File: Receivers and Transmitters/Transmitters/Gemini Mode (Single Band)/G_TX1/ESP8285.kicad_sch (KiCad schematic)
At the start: 22 parts, among them U4 ESP8285H16, Y2 26MHz

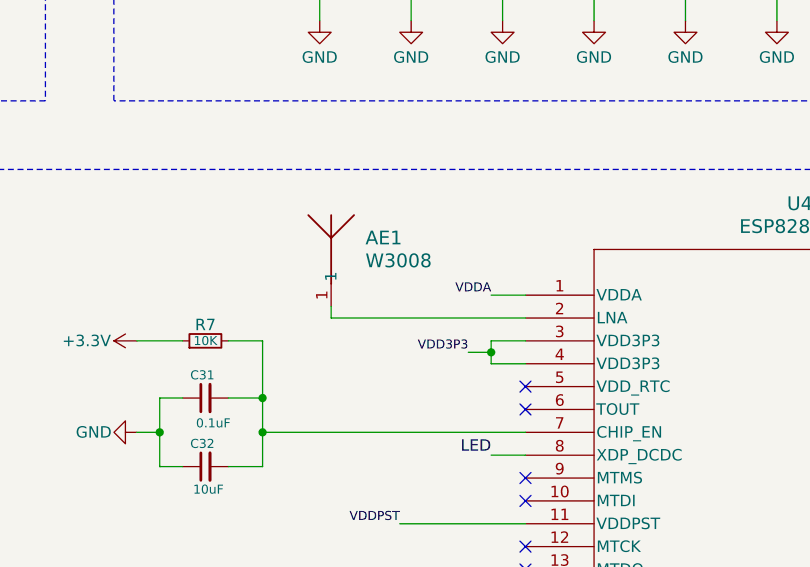
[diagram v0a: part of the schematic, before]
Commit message: Add Gemini Mode (Single Band) TX board image and documentation updates - Updated hardware setup to include Gemini TX - Added G_TX1_2.4G preview image - Updated KiCad schematic with LNA section and 5.6pF matching capacitor for 50Ω impedance - Modified PCB layout accordingly - Updated README and index.html with Gemini TX board references
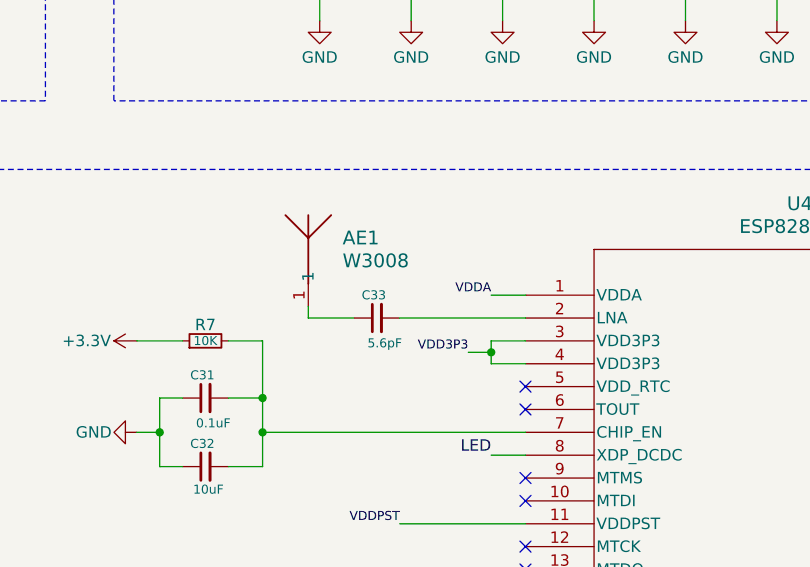
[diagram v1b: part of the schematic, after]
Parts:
- added C33: 5.6pF, Capacitor_SMD:C_01005_0402Metric_Pad0.57x0.30mm_HandSolder, symbol Device:C_Small
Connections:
- net at AE1.1: now also C33.1; no longer U4.2 (LNA)
- new net: C33.2, U4.2 (LNA)
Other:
- moved on the sheet: AE1
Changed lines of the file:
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@@
+	(wire
+		(pts
+			(xy 92.71 91.44) (xy 97.79 91.44)
+		)
+		(stroke
+			(width 0)
+			(type default)
+		)
+	)
 	(wire
 		(pts
@@
 	(wire
 		(pts
-			(xy 95.25 91.44) (xy 116.84 91.44)
-		)
-		(stroke
-			(width 0)
-			(type default)
-		)
-	)
-	(wire
-		(pts
 			(xy 78.74 107.95) (xy 76.2 107.95)
 		)
@@
 	(wire
 		(pts
+			(xy 102.87 91.44) (xy 116.84 91.44)
+		)
+		(stroke
+			(width 0)
+			(type default)
+		)
+	)
+	(wire
+		(pts
 			(xy 205.74 106.68) (xy 207.01 106.68)
 		)
@@
 	(wire
 		(pts
-			(xy 95.25 90.17) (xy 95.25 91.44)
+			(xy 92.71 90.17) (xy 92.71 91.44)
 		)
 		(stroke
@@
 	)
 	(symbol
+		(lib_id "Device:C_Small")
+		(at 100.33 91.44 90)
+		(unit 1)
+		(exclude_from_sim no)
+		(in_bom yes)
+		(on_board yes)
+		(dnp no)
+		(property "Reference" "C33"
+			(at 101.346 88.9 90)
+			(effects
+				(font
+					(size 1 1)
+				)
+				(justify left)
+			)
+		)
+		(property "Value" "5.6pF"
+			(at 103.124 94.234 90)
+			(effects
+				(font
+					(size 1 1)
+				)
+				(justify left)
+			)
+		)
+		(property "Footprint" "Capacitor_SMD:C_01005_0402Metric_Pad0.57x0.30mm_HandSolder"
+			(at 100.33 91.44 0)
+			(effects
+				(font
+					(size 1.27 1.27)
+				)
+				(hide yes)
+			)
+		)
+		(property "Datasheet" "~"
+			(at 100.33 91.44 0)
+			(effects
+				(font
+					(size 1.27 1.27)
+				)
+				(hide yes)
+			)
+		)
+		(property "Description" "Unpolarized capacitor, small symbol"
+			(at 100.33 91.44 0)
+			(effects
+				(font
+					(size 1.27 1.27)
+				)
+				(hide yes)
+			)
+		)
+		(pin "2"
+		)
+		(pin "1"
+		)
+		(instances
+			(project "G_TX1"
+				(path "/32640adb-d3ae-4079-8814-1903180e0e12/36e48682-81ba-44b4-b268-d93465b8c4e7"
+					(reference "C33")
+					(unit 1)
+				)
+			)
+		)
+	)
+	(symbol
 		(lib_id "Jumper:Jumper_2_Small_Bridged")
 		(at 101.6 137.16 270)
@@
 	(symbol
 		(lib_id "W3008:W3008")
-		(at 95.25 90.17 0)
+		(at 92.71 90.17 0)
 		(unit 1)
 		(exclude_from_sim no)
@@
 		(fields_autoplaced yes)
 		(property "Reference" "AE1"
-			(at 99.06 82.5499 0)
+			(at 96.52 82.5499 0)
 			(effects
 				(font
@@
 		)
 		(property "Value" "W3008"
-			(at 99.06 85.0899 0)
+			(at 96.52 85.0899 0)
 			(effects
 				(font
@@
 		)
 		(property "Footprint" "W3008:ANT_W3008_PUL"
-			(at 95.25 90.17 0)
+			(at 92.71 90.17 0)
 			(effects
 				(font
@@
 		)
 		(property "Datasheet" "W3008"
-			(at 95.25 90.17 0)
+			(at 92.71 90.17 0)
 			(effects
 				(font
@@
 		)
 		(property "Description" ""
-			(at 95.25 90.17 0)
-			(effects
-				(font
+			(at 92.71 90.17 0)
+			(effects
+				(font

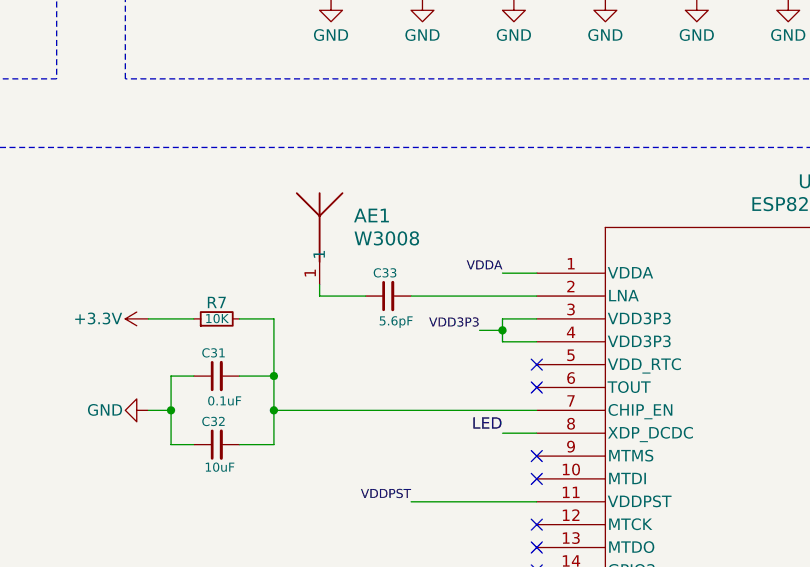
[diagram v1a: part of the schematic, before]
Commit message: Update Antenna Diversity (AD1_2.4G), True Antenna Diversity (TD1_2.4G), and Gemini Mode transmitter (G_TX1): Modify KiCad files, add BOMs and production files; update images, docs, videos, and README; remove outdated Mechanical CAD file
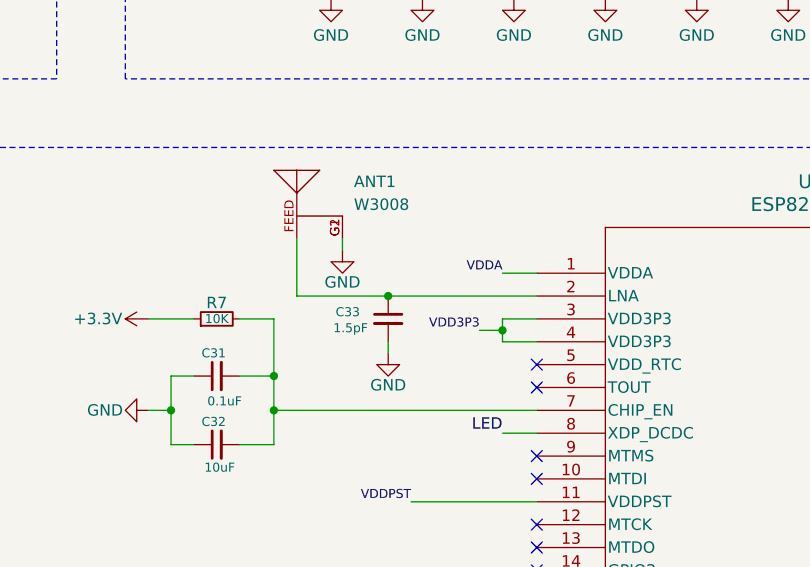
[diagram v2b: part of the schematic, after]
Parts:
- removed AE1: W3008, W3008:ANT_W3008_PUL, symbol W3008:W3008
- added ANT1: W3008, W3008:ANTENNA_W3008, symbol W3008:W3008
- C33: value 5.6pF -> 1.5pF
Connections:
- net GND: now also C33.2, ANT1.G1, ANT1.G2
- net at C33.1: now also U4.2 (LNA), ANT1.FEED
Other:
- company: https://github.com/Paschalis | TeodoraMiu -> https://github.com/Paschalis
- moved on the sheet: C33

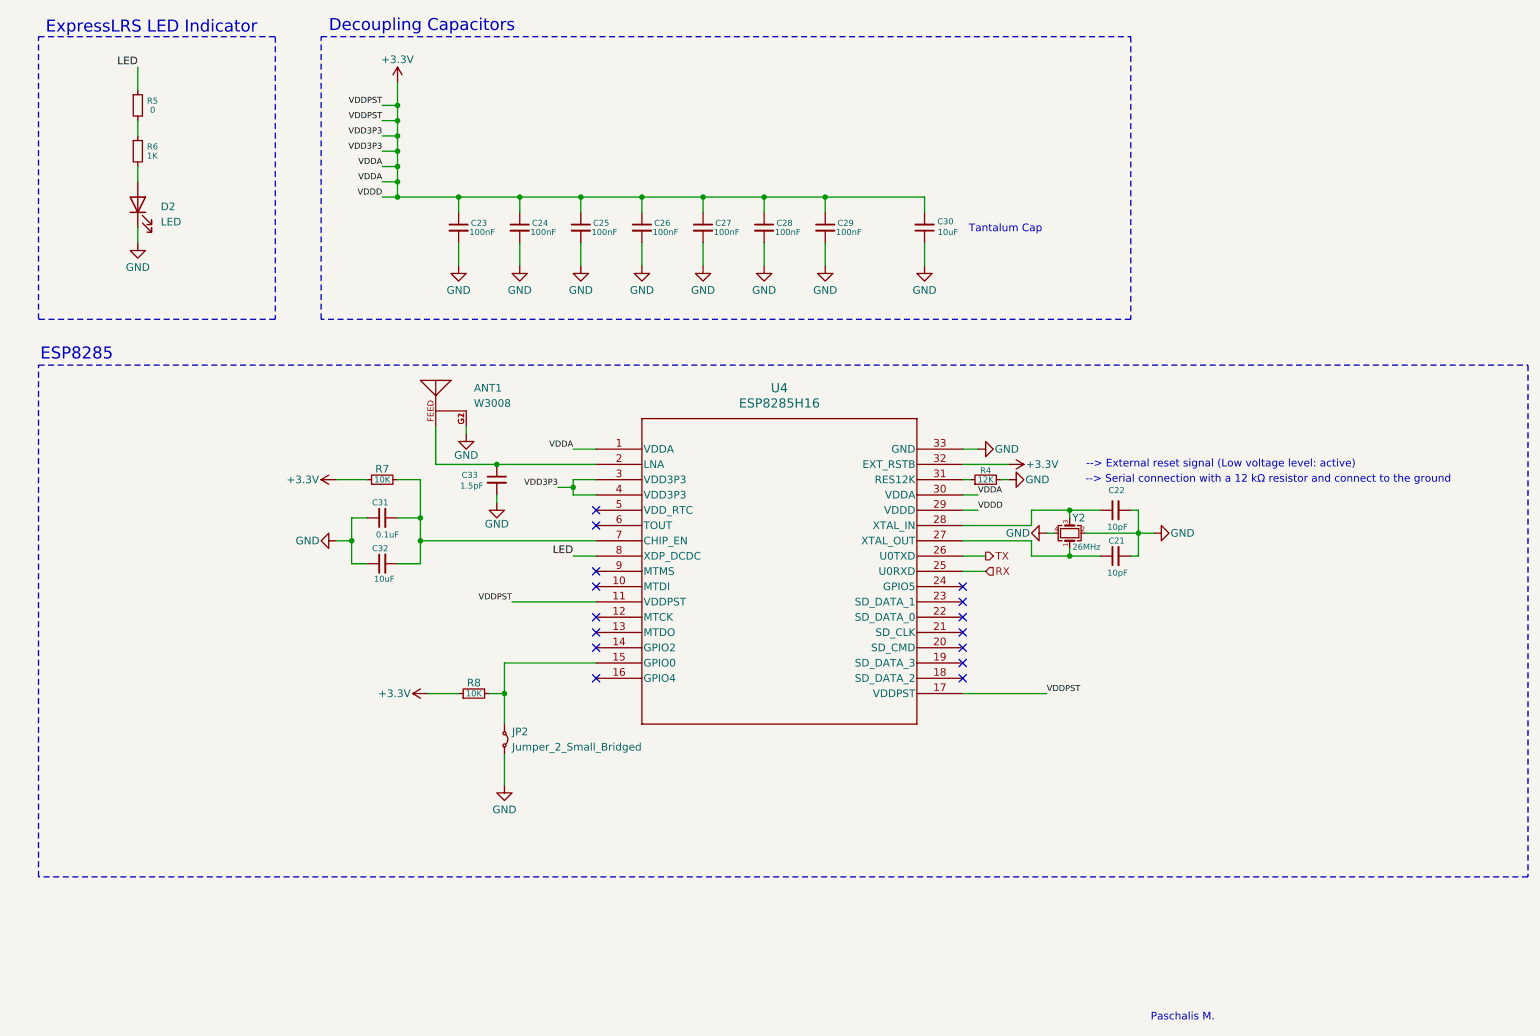
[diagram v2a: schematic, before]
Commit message: Update G_TX1 Freecad for enclosure and KiCad files (schematics, PCB, and project) - added fan pin headers
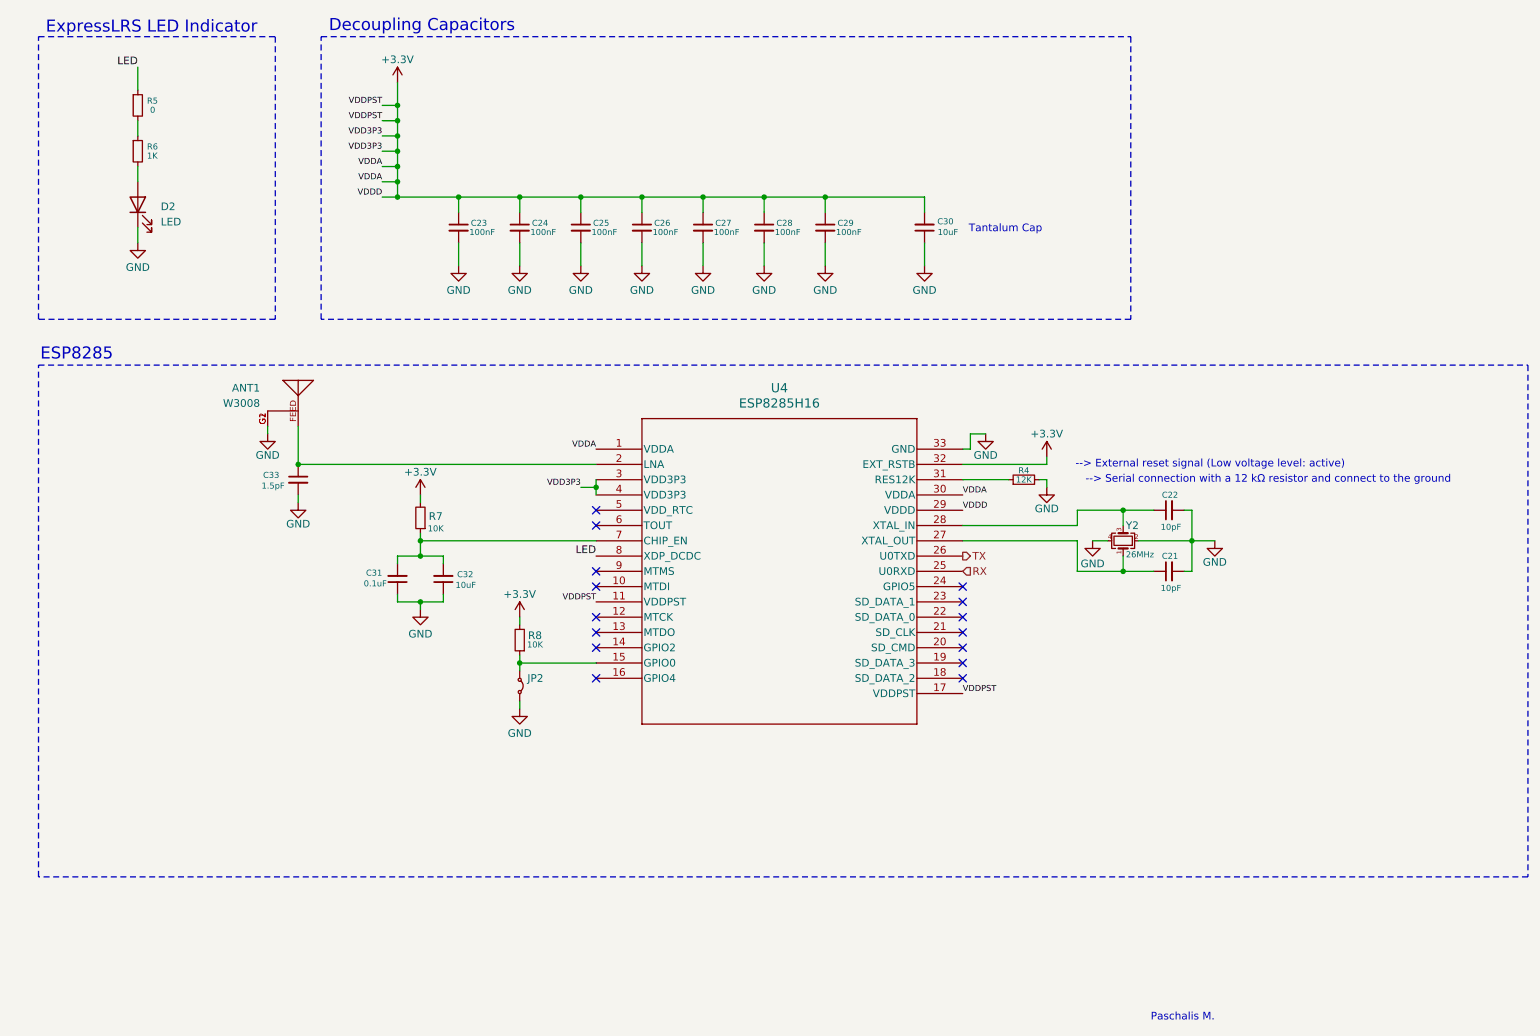
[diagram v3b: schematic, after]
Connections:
- net +3.3V: now also R7.2, R8.2; no longer R7.1, R8.1
- net at JP2.1 (A), U4.15 (GPIO0): now also R8.1; no longer R8.2
- net at C31.2, C32.2, U4.7 (CHIP_EN): now also R7.1; no longer R7.2
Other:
- moved on the sheet: ANT1, C21, C22, C31, C32, C33, JP2, R4, R7, R8, Y2
